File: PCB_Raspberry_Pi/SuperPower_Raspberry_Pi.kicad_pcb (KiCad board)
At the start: 2 copper layers, 65 x 56 mm, 5 parts, among them J1 RPi_GPIO

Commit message: libraries organized
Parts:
- removed ? (x4): , RPi_Hat:RPi_Hat_Mounting_Hole
- added H1: MountingHole, SuperPower_Library:RPi_Hat_Mounting_Hole, F.Cu at (114.0, 113.5)
- added H2: MountingHole, SuperPower_Library:RPi_Hat_Mounting_Hole, F.Cu at (172.0, 113.5)
- added H3: MountingHole, SuperPower_Library:RPi_Hat_Mounting_Hole, F.Cu at (172.0, 64.5)
- added H4: MountingHole, SuperPower_Library:RPi_Hat_Mounting_Hole, F.Cu at (114.0, 64.5)
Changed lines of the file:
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@@
     (add_net GND)
-  )
-  (module RPi_Hat:RPi_Hat_Mounting_Hole locked (layer F.Cu)
-    (at 171.99 64.452)
-    (descr "Mounting hole, Befestigungsbohrung, 2,7mm, No Annular, Kein Restring,")
-    (tags "Mounting hole, Befestigungsbohrung, 2,7mm, No Annular, Kein Restring,")
-    (fp_text reference "" (at 0 -4.0005) (layer F.SilkS) hide
-      (effects (font (size 1 1) (thickness 0.15)))
-    )
-    (fp_text value "" (at 0.09906 3.59918) (layer F.Fab) hide
-      (effects (font (size 1 1) (thickness 0.15)))
-    )
-    (fp_circle (center 0 0) (end 1.375 0) (layer F.Fab) (width 0.15))
-    (fp_circle (center 0 0) (end 3.1 0) (layer F.Fab) (width 0.15))
-    (fp_circle (center 0 0) (end 3.1 0) (layer B.Fab) (width 0.15))
-    (fp_circle (center 0 0) (end 1.375 0) (layer B.Fab) (width 0.15))
-    (fp_circle (center 0 0) (end 3.1 0) (layer F.CrtYd) (width 0.15))
-    (fp_circle (center 0 0) (end 3.1 0) (layer B.CrtYd) (width 0.15))
-    (pad "" np_thru_hole circle (at 0 0) (size 2.75 2.75) (drill 2.75) (layers *.Cu *.Mask)
-      (solder_mask_margin 1.725) (clearance 1.725))
-  )
-  (module RPi_Hat:RPi_Hat_Mounting_Hole locked (layer F.Cu)
-    (at 171.99 113.452)
-    (descr "Mounting hole, Befestigungsbohrung, 2,7mm, No Annular, Kein Restring,")
-    (tags "Mounting hole, Befestigungsbohrung, 2,7mm, No Annular, Kein Restring,")
-    (fp_text reference "" (at 0 -4.0005) (layer F.SilkS) hide
-      (effects (font (size 1 1) (thickness 0.15)))
-    )
-    (fp_text value "" (at 0.09906 3.59918) (layer F.Fab) hide
-      (effects (font (size 1 1) (thickness 0.15)))
-    )
-    (fp_circle (center 0 0) (end 1.375 0) (layer F.Fab) (width 0.15))
-    (fp_circle (center 0 0) (end 3.1 0) (layer F.Fab) (width 0.15))
-    (fp_circle (center 0 0) (end 3.1 0) (layer B.Fab) (width 0.15))
-    (fp_circle (center 0 0) (end 1.375 0) (layer B.Fab) (width 0.15))
-    (fp_circle (center 0 0) (end 3.1 0) (layer F.CrtYd) (width 0.15))
-    (fp_circle (center 0 0) (end 3.1 0) (layer B.CrtYd) (width 0.15))
-    (pad "" np_thru_hole circle (at 0 0) (size 2.75 2.75) (drill 2.75) (layers *.Cu *.Mask)
-      (solder_mask_margin 1.725) (clearance 1.725))
-  )
-  (module RPi_Hat:RPi_Hat_Mounting_Hole locked (layer F.Cu)
-    (at 113.99 113.452)
-    (descr "Mounting hole, Befestigungsbohrung, 2,7mm, No Annular, Kein Restring,")
-    (tags "Mounting hole, Befestigungsbohrung, 2,7mm, No Annular, Kein Restring,")
-    (fp_text reference "" (at 0 -4.0005) (layer F.SilkS) hide
-      (effects (font (size 1 1) (thickness 0.15)))
-    )
-    (fp_text value "" (at 0.09906 3.59918) (layer F.Fab) hide
-      (effects (font (size 1 1) (thickness 0.15)))
-    )
-    (fp_circle (center 0 0) (end 1.375 0) (layer F.Fab) (width 0.15))
-    (fp_circle (center 0 0) (end 3.1 0) (layer F.Fab) (width 0.15))
-    (fp_circle (center 0 0) (end 3.1 0) (layer B.Fab) (width 0.15))
-    (fp_circle (center 0 0) (end 1.375 0) (layer B.Fab) (width 0.15))
-    (fp_circle (center 0 0) (end 3.1 0) (layer F.CrtYd) (width 0.15))
-    (fp_circle (center 0 0) (end 3.1 0) (layer B.CrtYd) (width 0.15))
-    (pad "" np_thru_hole circle (at 0 0) (size 2.75 2.75) (drill 2.75) (layers *.Cu *.Mask)
-      (solder_mask_margin 1.725) (clearance 1.725))
-  )
-  (module RPi_Hat:RPi_Hat_Mounting_Hole locked (layer F.Cu)
-    (at 113.99 64.452)
-    (descr "Mounting hole, Befestigungsbohrung, 2,7mm, No Annular, Kein Restring,")
-    (tags "Mounting hole, Befestigungsbohrung, 2,7mm, No Annular, Kein Restring,")
-    (fp_text reference "" (at 0 -4.0005) (layer F.SilkS) hide
-      (effects (font (size 1 1) (thickness 0.15)))
-    )
-    (fp_text value "" (at 0.09906 3.59918) (layer F.Fab) hide
-      (effects (font (size 1 1) (thickness 0.15)))
-    )
-    (fp_circle (center 0 0) (end 1.375 0) (layer F.Fab) (width 0.15))
-    (fp_circle (center 0 0) (end 3.1 0) (layer F.Fab) (width 0.15))
-    (fp_circle (center 0 0) (end 3.1 0) (layer B.Fab) (width 0.15))
-    (fp_circle (center 0 0) (end 1.375 0) (layer B.Fab) (width 0.15))
-    (fp_circle (center 0 0) (end 3.1 0) (layer F.CrtYd) (width 0.15))
-    (fp_circle (center 0 0) (end 3.1 0) (layer B.CrtYd) (width 0.15))
-    (pad "" np_thru_hole circle (at 0 0) (size 2.75 2.75) (drill 2.75) (layers *.Cu *.Mask)
-      (solder_mask_margin 1.725) (clearance 1.725))
   )
   (module Connector_PinSocket_2.54mm:PinSocket_2x20_P2.54mm_Vertical (layer B.Cu)
@@
     )
   )
+  (module SuperPower_Library:RPi_Hat_Mounting_Hole locked (layer F.Cu)
+    (at 113.99 113.452)
+    (descr "Mounting hole, Befestigungsbohrung, 2,7mm, No Annular, Kein Restring,")
+    (tags "Mounting hole, Befestigungsbohrung, 2,7mm, No Annular, Kein Restring,")
+    (fp_text reference H1 (at 0 -4.0005) (layer F.SilkS) hide
+      (effects (font (size 1 1) (thickness 0.15)))
+    )
+    (fp_text value MountingHole (at 0.09906 3.59918) (layer F.Fab) hide
+      (effects (font (size 1 1) (thickness 0.15)))
+    )
+    (fp_circle (center 0 0) (end 3.1 0) (layer B.CrtYd) (width 0.15))
+    (fp_circle (center 0 0) (end 3.1 0) (layer F.CrtYd) (width 0.15))
+    (fp_circle (center 0 0) (end 1.375 0) (layer B.Fab) (width 0.15))
+    (fp_circle (center 0 0) (end 3.1 0) (layer B.Fab) (width 0.15))
+    (fp_circle (center 0 0) (end 3.1 0) (layer F.Fab) (width 0.15))
+    (fp_circle (center 0 0) (end 1.375 0) (layer F.Fab) (width 0.15))
+    (pad "" np_thru_hole circle (at 0 0) (size 2.75 2.75) (drill 2.75) (layers *.Cu *.Mask)
+      (solder_mask_margin 1.725) (clearance 1.725))
+  )
+  (module SuperPower_Library:RPi_Hat_Mounting_Hole locked (layer F.Cu)
+    (at 171.99 113.452)
+    (descr "Mounting hole, Befestigungsbohrung, 2,7mm, No Annular, Kein Restring,")
+    (tags "Mounting hole, Befestigungsbohrung, 2,7mm, No Annular, Kein Restring,")
+    (fp_text reference H2 (at 0 -4.0005) (layer F.SilkS) hide
+      (effects (font (size 1 1) (thickness 0.15)))
+    )
+    (fp_text value MountingHole (at 0.09906 3.59918) (layer F.Fab) hide
+      (effects (font (size 1 1) (thickness 0.15)))
+    )
+    (fp_circle (center 0 0) (end 1.375 0) (layer F.Fab) (width 0.15))
+    (fp_circle (center 0 0) (end 3.1 0) (layer F.Fab) (width 0.15))
+    (fp_circle (center 0 0) (end 3.1 0) (layer B.Fab) (width 0.15))
+    (fp_circle (center 0 0) (end 1.375 0) (layer B.Fab) (width 0.15))
+    (fp_circle (center 0 0) (end 3.1 0) (layer F.CrtYd) (width 0.15))
+    (fp_circle (center 0 0) (end 3.1 0) (layer B.CrtYd) (width 0.15))
+    (pad "" np_thru_hole circle (at 0 0) (size 2.75 2.75) (drill 2.75) (layers *.Cu *.Mask)
+      (solder_mask_margin 1.725) (clearance 1.725))
+  )
+  (module SuperPower_Library:RPi_Hat_Mounting_Hole locked (layer F.Cu)
+    (at 171.99 64.452)
+    (descr "Mounting hole, Befestigungsbohrung, 2,7mm, No Annular, Kein Restring,")
+    (tags "Mounting hole, Befestigungsbohrung, 2,7mm, No Annular, Kein Restring,")
+    (fp_text reference H3 (at 0 -4.0005) (layer F.SilkS) hide
+      (effects (font (size 1 1) (thickness 0.15)))
+    )
+    (fp_text value MountingHole (at 0.09906 3.59918) (layer F.Fab) hide
+      (effects (font (size 1 1) (thickness 0.15)))
+    )
+    (fp_circle (center 0 0) (end 3.1 0) (layer B.CrtYd) (width 0.15))
+    (fp_circle (center 0 0) (end 3.1 0) (layer F.CrtYd) (width 0.15))
+    (fp_circle (center 0 0) (end 1.375 0) (layer B.Fab) (width 0.15))
+    (fp_circle (center 0 0) (end 3.1 0) (layer B.Fab) (width 0.15))
+    (fp_circle (center 0 0) (end 3.1 0) (layer F.Fab) (width 0.15))
+    (fp_circle (center 0 0) (end 1.375 0) (layer F.Fab) (width 0.15))
+    (pad "" np_thru_hole circle (at 0 0) (size 2.75 2.75) (drill 2.75) (layers *.Cu *.Mask)
+      (solder_mask_margin 1.725) (clearance 1.725))
+  )
+  (module SuperPower_Library:RPi_Hat_Mounting_Hole locked (layer F.Cu)
+    (at 113.99 64.452)
+    (descr "Mounting hole, Befestigungsbohrung, 2,7mm, No Annular, Kein Restring,")
+    (tags "Mounting hole, Befestigungsbohrung, 2,7mm, No Annular, Kein Restring,")
+    (fp_text reference H4 (at 0 -4.0005) (layer F.SilkS) hide
+      (effects (font (size 1 1) (thickness 0.15)))
+    )
+    (fp_text value MountingHole (at 0.09906 3.59918) (layer F.Fab) hide
+      (effects (font (size 1 1) (thickness 0.15)))
+    )
+    (fp_circle (center 0 0) (end 1.375 0) (layer F.Fab) (width 0.15))
+    (fp_circle (center 0 0) (end 3.1 0) (layer F.Fab) (width 0.15))
+    (fp_circle (center 0 0) (end 3.1 0) (layer B.Fab) (width 0.15))
+    (fp_circle (center 0 0) (end 1.375 0) (layer B.Fab) (width 0.15))
+    (fp_circle (center 0 0) (end 3.1 0) (layer F.CrtYd) (width 0.15))
+    (fp_circle (center 0 0) (end 3.1 0) (layer B.CrtYd) (width 0.15))
+    (pad "" np_thru_hole circle (at 0 0) (size 2.75 2.75) (drill 2.75) (layers *.Cu *.Mask)
+      (solder_mask_margin 1.725) (clearance 1.725))
+  )
   (gr_text "Select one of these board edges depending \nupon the type of socket that is used." (at 192.99 60.952) (layer Cmts.User)
     (effects (font (size 1.5 1.5) (thickness 0.15)) (justify left))
@@
   (gr_line (start 113.49 116.952) (end 172.49 116.952) (angle 90) (layer Edge.Cuts) (width 0.1))
   (gr_line (start 175.49 63.952) (end 175.49 113.952) (angle 90) (layer Edge.Cuts) (width 0.1))
-  (segment (start 118.8212 63.1698) (end 121.3612 63.1698) (width 0.381) (layer F.Cu) (net 2))
+  (segment (start 118.8212 63.1698) (end 121.3612 63.1698) (width 0.381) (layer F.Cu) (net 2) (status 30))
   (zone (net 1) (net_name GND) (layer B.Cu) (hatch edge 0.508)
     (connect_pads (clearance 0.508))

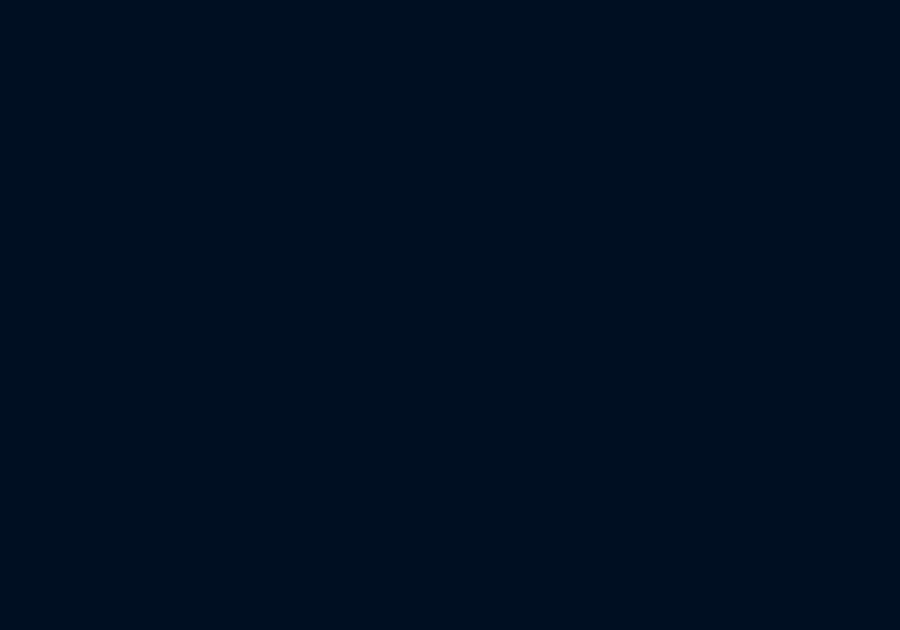
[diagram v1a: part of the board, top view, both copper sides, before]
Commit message: script for export BOM
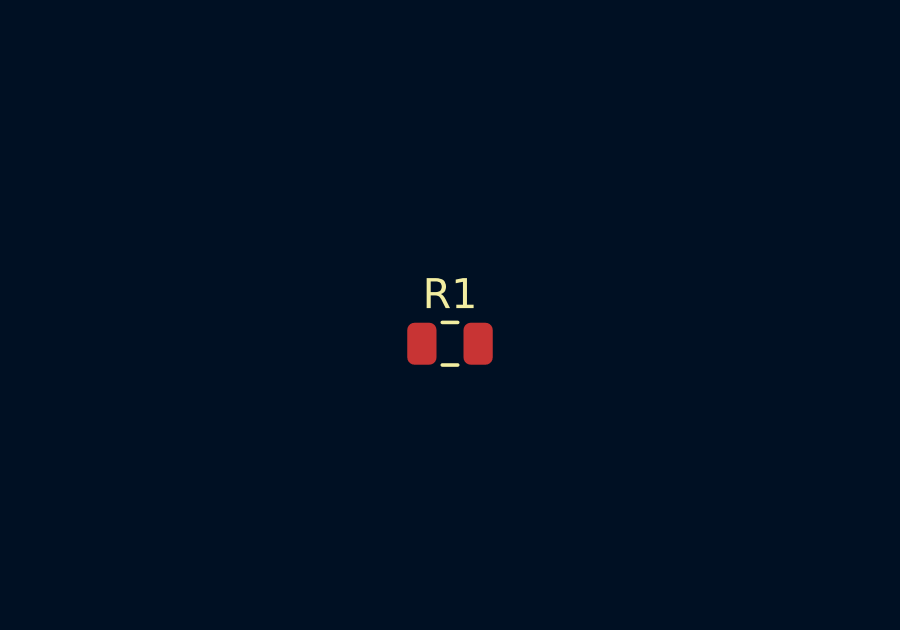
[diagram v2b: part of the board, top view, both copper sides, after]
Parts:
- added R1: 1k, Resistor_SMD:R_0805_2012Metric, F.Cu at (148.1, 89.9)
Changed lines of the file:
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@@
-(kicad_pcb (version 20171130) (host pcbnew 5.0.2-bee76a0~70~ubuntu16.04.1)
+(kicad_pcb (version 20171130) (host pcbnew 5.1.6-c6e7f7d~87~ubuntu16.04.1)
   (general
     (thickness 1.6)
@@
     (tracks 1)
     (zones 0)
-    (modules 5)
+    (modules 6)
     (nets 3)
   )
@@
     (zone_45_only no)
     (trace_min 0.01)
-    (segment_width 0.2)
-    (edge_width 0.1)
     (via_size 0.6)
     (via_drill 0.4)
@@
     (uvia_min_size 0.2)
     (uvia_min_drill 0.1)
+    (edge_width 0.1)
+    (segment_width 0.2)
     (pcb_text_width 0.3)
     (pcb_text_size 1.5 1.5)
@@
       (solder_mask_margin 1.725) (clearance 1.725))
   )
+  (module Resistor_SMD:R_0805_2012Metric (layer F.Cu)
+    (at 148.082 89.916)
+    (descr "Resistor SMD 0805 (2012 Metric), square (rectangular) end terminal, IPC_7351 nominal, (Body size source: https://docs.google.com/spreadsheets/d/1BsfQQcO9C6DZCsRaXUlFlo91Tg2WpOkGARC1WS5S8t0/edit?usp=sharing), generated with kicad-footprint-generator")
+    (tags resistor)
+    (attr smd)
+    (fp_text reference R1 (at 0 -1.65) (layer F.SilkS)
+      (effects (font (size 1 1) (thickness 0.15)))
+    )
+    (fp_text value 1k (at 0 1.65) (layer F.Fab)
+      (effects (font (size 1 1) (thickness 0.15)))
+    )
+    (fp_line (start -1 0.6) (end -1 -0.6) (layer F.Fab) (width 0.1))
+    (fp_line (start -1 -0.6) (end 1 -0.6) (layer F.Fab) (width 0.1))
+    (fp_line (start 1 -0.6) (end 1 0.6) (layer F.Fab) (width 0.1))
+    (fp_line (start 1 0.6) (end -1 0.6) (layer F.Fab) (width 0.1))
+    (fp_line (start -0.258578 -0.71) (end 0.258578 -0.71) (layer F.SilkS) (width 0.12))
+    (fp_line (start -0.258578 0.71) (end 0.258578 0.71) (layer F.SilkS) (width 0.12))
+    (fp_line (start -1.68 0.95) (end -1.68 -0.95) (layer F.CrtYd) (width 0.05))
+    (fp_line (start -1.68 -0.95) (end 1.68 -0.95) (layer F.CrtYd) (width 0.05))
+    (fp_line (start 1.68 -0.95) (end 1.68 0.95) (layer F.CrtYd) (width 0.05))
+    (fp_line (start 1.68 0.95) (end -1.68 0.95) (layer F.CrtYd) (width 0.05))
+    (fp_text user %R (at 0 0) (layer F.Fab)
+      (effects (font (size 0.5 0.5) (thickness 0.08)))
+    )
+    (pad 1 smd roundrect (at -0.9375 0) (size 0.975 1.4) (layers F.Cu F.Paste F.Mask) (roundrect_rratio 0.25))
+    (pad 2 smd roundrect (at 0.9375 0) (size 0.975 1.4) (layers F.Cu F.Paste F.Mask) (roundrect_rratio 0.25))
+    (model ${KISYS3DMOD}/Resistor_SMD.3dshapes/R_0805_2012Metric.wrl
+      (at (xyz 0 0 0))
+      (scale (xyz 1 1 1))
+      (rotate (xyz 0 0 0))
+    )
+  )
   (module SuperPower_Library:RPi_Hat_Mounting_Hole locked (layer F.Cu)
